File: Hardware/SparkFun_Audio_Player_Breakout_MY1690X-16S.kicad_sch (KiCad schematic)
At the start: 41 parts, among them J1 3.5mm TRRS, J2 Conn_01x03, J3 Conn_01x02, J4 USB_C_Receptacle, J5 Conn_01x06, J6 microSD, Q1 BSS138, U2 MY1690X-16S

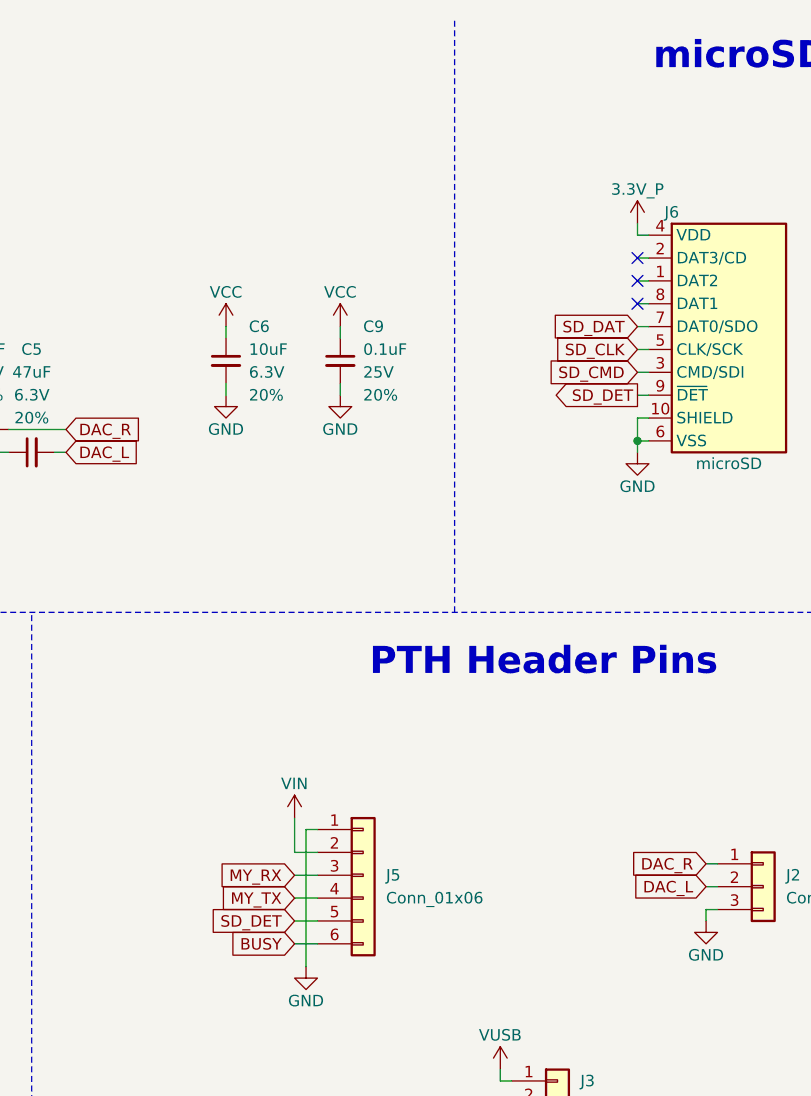
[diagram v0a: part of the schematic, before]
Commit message: Post-proto testing changes - v10
-bumped version to v10 in sch and brd
-added 3.4-5V in buzzard labels at the header pin
-added over-bar to sd detect silk
-added pullup resistor on sd detect
-Move 3.3V_P trace elsewhere to avoid coupling and keep a complete plane (VCC) under the USB D+/D- lines.
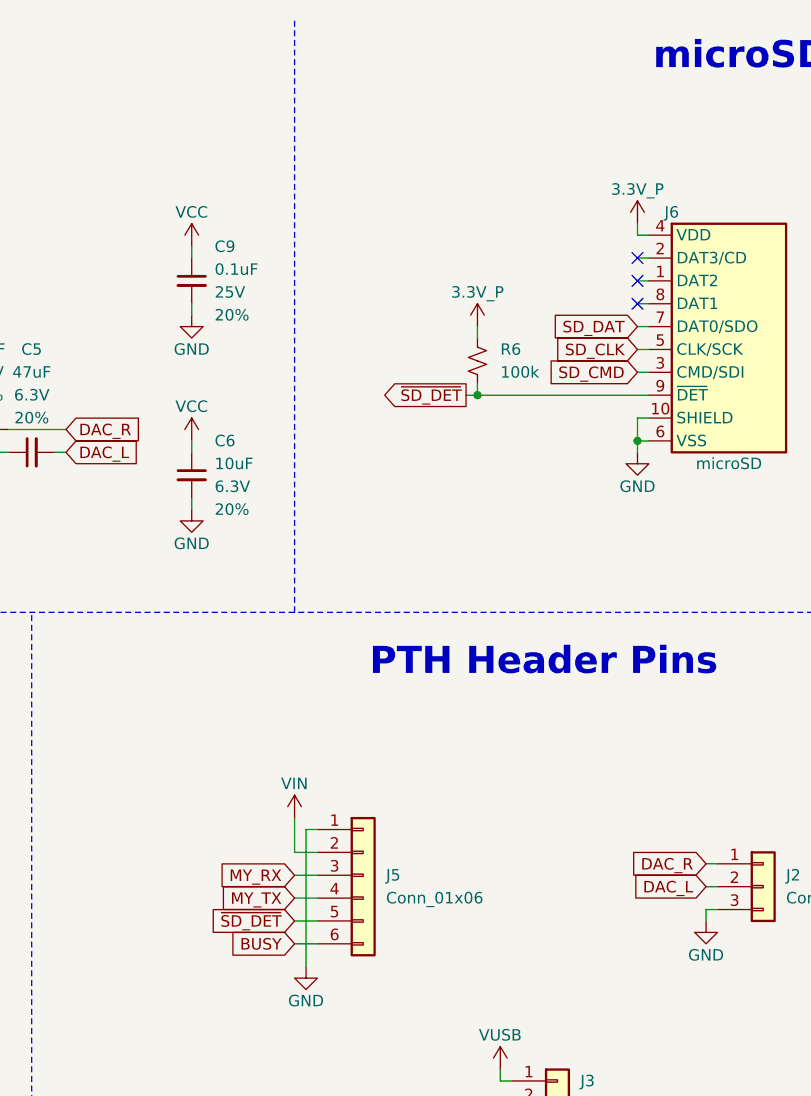
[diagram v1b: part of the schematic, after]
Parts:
- added R6: 100k, SparkFun-Resistor:R_0603_1608Metric, symbol SparkFun-Resistor:100k_0603
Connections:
- net 3.3V_P: now also R6.1
- net SD_DET renamed ~{SD_DET}
- net ~{SD_DET}: now also R6.2
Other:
- moved on the sheet: C6, C9

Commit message: Sch cleanup
-change title block texts to standard color and boldness
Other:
- note added: "Audio Player IC"
- note added: "micro SD Socket"
- note removed: "Audio Player"
- note removed: "microSD"
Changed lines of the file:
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@@
+		)
+	)
+	(text "USBC"
+		(exclude_from_sim no)
+		(at 35.56 17.78 0)
+		(effects
+			(font
+				(size 3 3)
+			)
+		)
+	)
+	(text "Serial Conversion"
+		(exclude_from_sim no)
+		(at 121.92 86.36 0)
+		(effects
+			(font
+				(size 3 3)
+			)
 		)
 	)
 	(text "MY1609 requires 3.4V to 5V"
 		(exclude_from_sim no)
-		(at 126.238 21.082 0)
+		(at 127 24.13 0)
 		(effects
 			(font
@@
 		)
 	)
-	(text "Serial Conversion"
+	(text "Audio Output (3.5mm TRRS)"
 		(exclude_from_sim no)
-		(at 122.682 86.106 0)
+		(at 50.8 86.36 0)
 		(effects
 			(font
 				(size 3 3)
-				(thickness 0.6)
-				(bold yes)
-				(color 132 0 0 1)
-			)
-		)
-	)
-	(text "Audio Output (3.5mm TRRS)"
-		(exclude_from_sim no)
-		(at 49.022 85.344 0)
-		(effects
-			(font
-				(size 3 3)
-				(thickness 0.6)
-				(bold yes)
-				(color 132 0 0 1)
 			)
 		)
@@
 		)
 	)
-	(text "USBC"
+	(text "micro SD Socket"
 		(exclude_from_sim no)
-		(at 35.052 17.272 0)
+		(at 226.06 17.78 0)
 		(effects
 			(font
 				(size 3 3)
-				(thickness 0.6)
-				(bold yes)
-				(color 132 0 0 1)
 			)
 		)
 	)
-	(text "microSD"
+	(text "Power Input"
 		(exclude_from_sim no)
-		(at 237.49 17.018 0)
+		(at 48.26 151.13 0)
 		(effects
 			(font
 				(size 3 3)
-				(thickness 0.6)
-				(bold yes)
-				(color 132 0 0 1)
 			)
 		)
 	)
-	(text "Audio Player"
+	(text "PTH Header Pins"
 		(exclude_from_sim no)
-		(at 126.238 17.272 0)
+		(at 213.36 86.36 0)
 		(effects
 			(font
 				(size 3 3)
-				(thickness 0.6)
-				(bold yes)
-				(color 132 0 0 1)
+			)
+		)
+	)
+	(text "Audio Player IC"
+		(exclude_from_sim no)
+		(at 127 17.78 0)
+		(effects
+			(font
+				(size 3 3)
+			)
+		)
+	)
+	(text "LEDs"
+		(exclude_from_sim no)
+		(at 125.73 151.13 0)
+		(effects
+			(font
+				(size 3 3)
 			)
 		)
@@
 	(text "VIN: 3.4V to 5V"
 		(exclude_from_sim no)
-		(at 47.752 154.432 0)
+		(at 48.26 156.21 0)
 		(effects
 			(font
@@
 			)
 		)
-	)
-	(text "Power Input"
-		(exclude_from_sim no)
-		(at 47.752 149.606 0)
-		(effects
-			(font
-				(size 3 3)
-				(thickness 0.6)
-				(bold yes)
-				(color 132 0 0 1)
-			)
-		)
-	)
-	(text "PTH Header Pins"
-		(exclude_from_sim no)
-		(at 215.646 84.328 0)
-		(effects
-			(font
-				(size 3 3)
-				(thickness 0.6)
-				(bold yes)
-				(color 132 0 0 1)
-			)
-		)
-	)
-	(text "LEDs"
-		(exclude_from_sim no)
-		(at 125.222 150.368 0)
-		(effects
-			(font
-				(size 3 3)
-				(thickness 0.6)
-				(bold yes)
-				(color 132 0 0 1)
-			)
-		)
